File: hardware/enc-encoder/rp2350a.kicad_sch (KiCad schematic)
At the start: 35 parts, among them U1 RP2350A, U2 W25Q128JVS, Y1 ABM8-272-T3

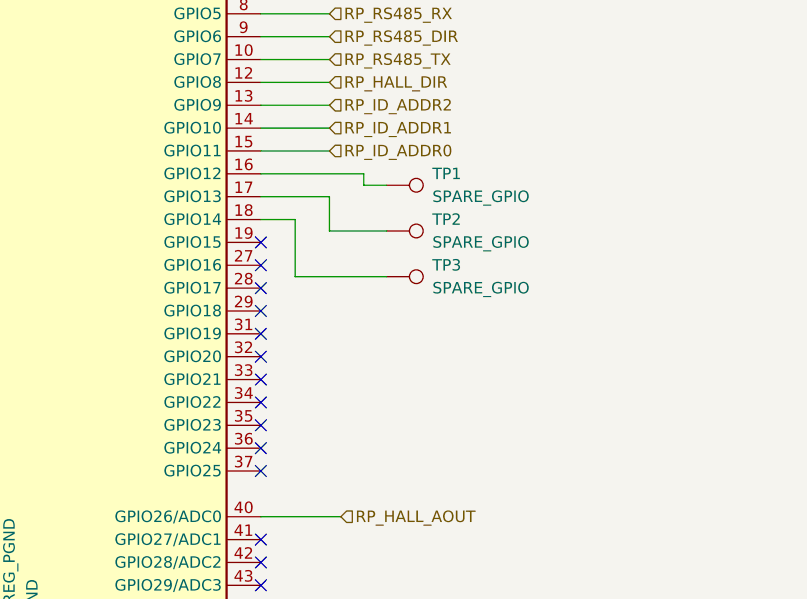
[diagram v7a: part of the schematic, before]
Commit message: Feat: Fixed USB High-speed trace matching
Fixed USB trace length matching for high-speed data communications.
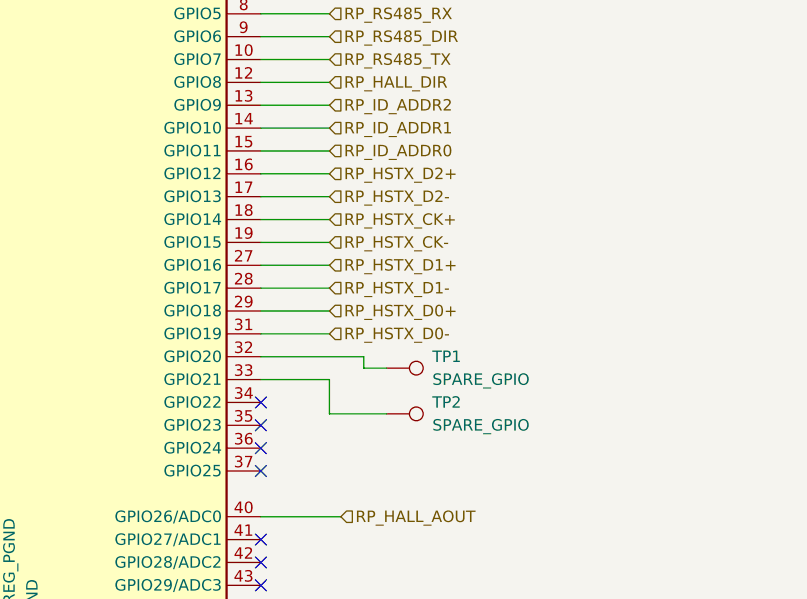
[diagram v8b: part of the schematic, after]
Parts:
- removed TP3: SPARE_GPIO, TestPoint:TestPoint_Pad_D1.0mm, symbol Connector:TestPoint
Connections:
- net at TP1.1: now also U1.32 (GPIO20); no longer U1.16 (GPIO12)
- net at TP2.1: now also U1.33 (GPIO21); no longer U1.17 (GPIO13)
- net RP_HSTX_CK+: now reaches U1.18 (GPIO14)
- net RP_HSTX_CK-: now reaches U1.19 (GPIO15)
- net RP_HSTX_D1+: now reaches U1.27 (GPIO16)
- net RP_HSTX_D1-: now reaches U1.28 (GPIO17)
- net RP_HSTX_D0+: now reaches U1.29 (GPIO18)
- net RP_HSTX_D0-: now reaches U1.31 (GPIO19)
- new net RP_HSTX_D2+: U1.16 (GPIO12)
- new net RP_HSTX_D2-: U1.17 (GPIO13)
- no-connect marks 14 -> 7
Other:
- moved on the sheet: TP1, TP2
